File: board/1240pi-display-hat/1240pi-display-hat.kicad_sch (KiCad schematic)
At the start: 7 parts, among them J1 SFV10R-1ST, P208 Header, P415 Header, U1 74F126, U208 74F04, U415 74S74

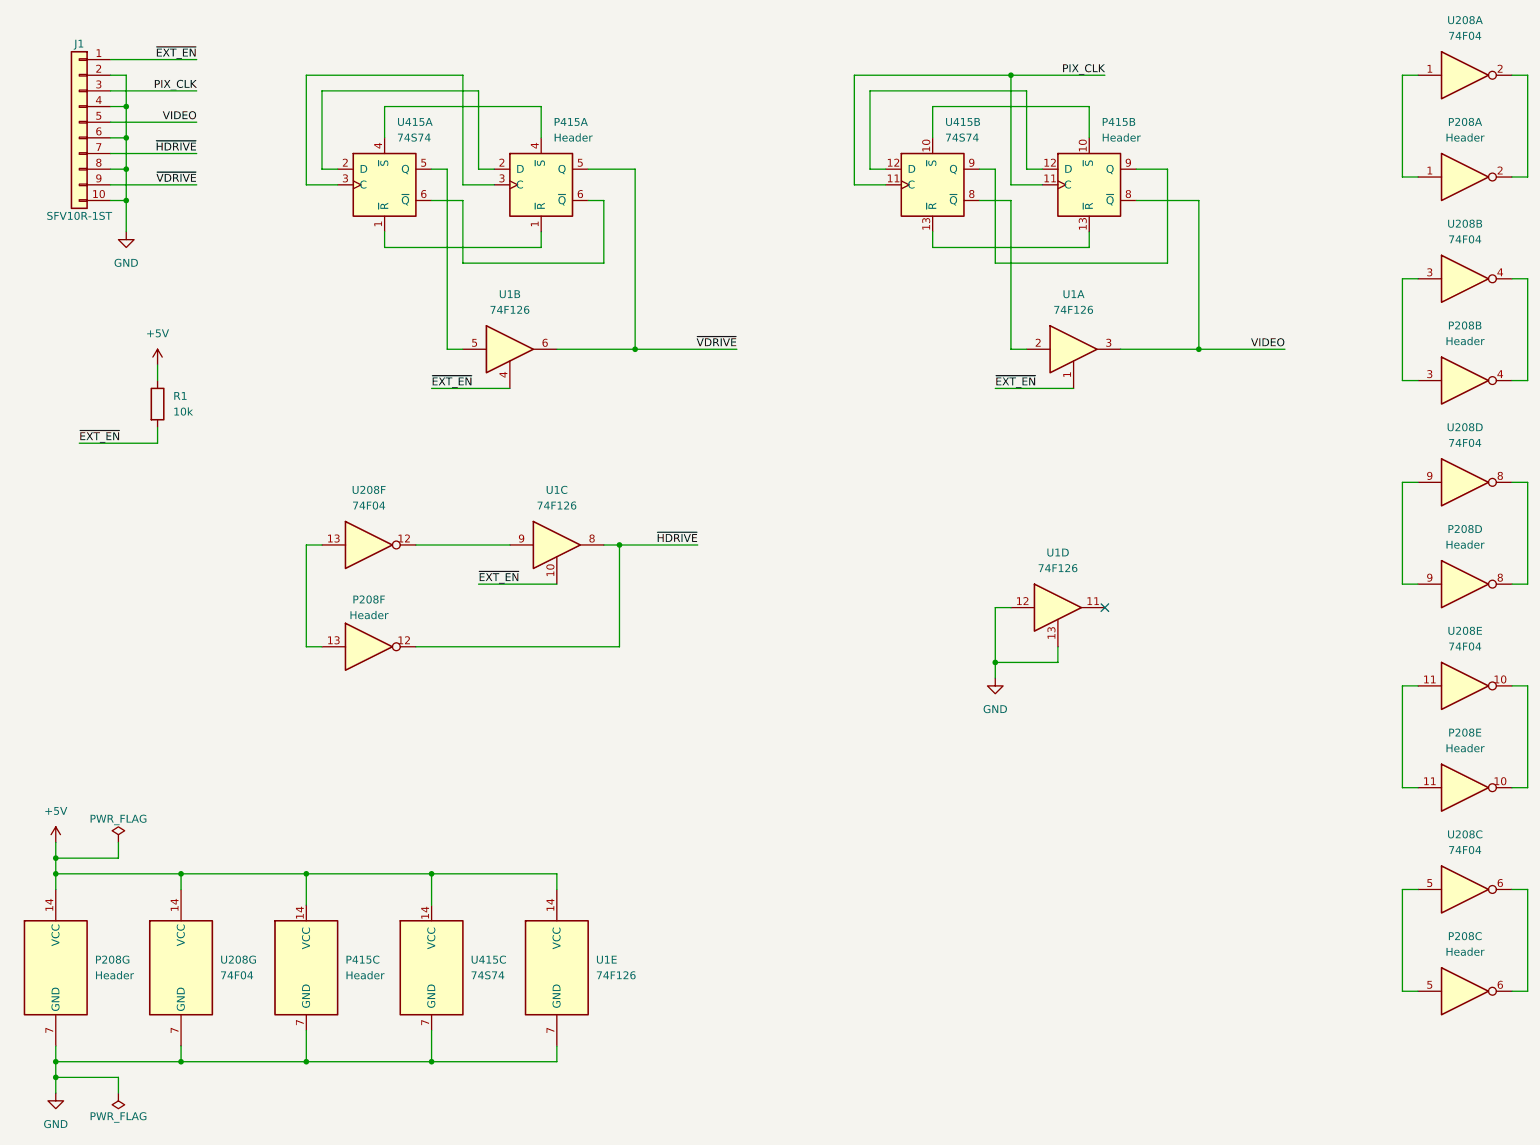
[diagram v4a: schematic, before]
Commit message: Use correct pin of U208 in display hay.
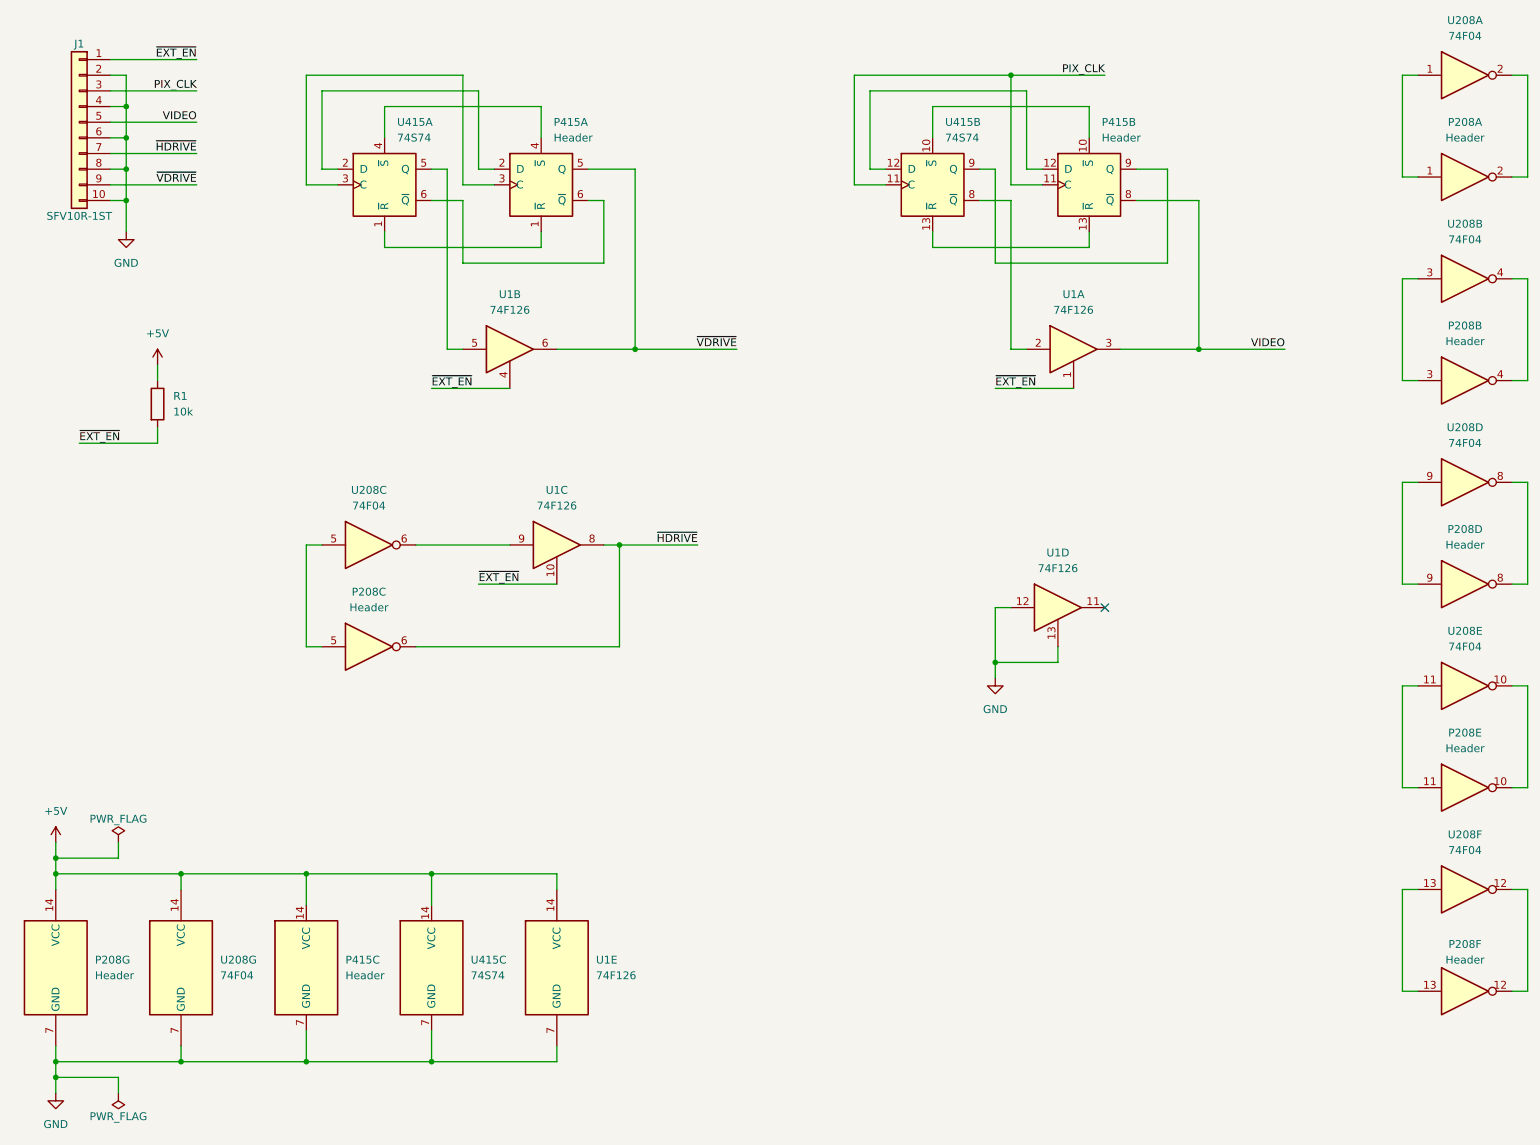
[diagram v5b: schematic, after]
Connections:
- net ~{HDRIVE}: now also P208.6; no longer P208.12
- net at U208.6: now also U1.9; no longer P208.6
- net at U208.12: now also P208.12; no longer U1.9
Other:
- moved on the sheet: P208C, P208F, U208C, U208F

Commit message: Convert display board hat to 3v3.
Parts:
- added C101, C102: 22u, Capacitor_SMD:C_0805_2012Metric, symbol Device:C_Small
- added U101: AP1117-33, Package_TO_SOT_SMD:SOT-223-3_TabPin2, symbol Regulator_Linear:AP1117-33
- U1: value 74F126 -> 74LVC126; footprint Package_DIP:DIP-14_W7.62mm -> Package_SO:SO-14_3.9x8.65mm_P1.27mm
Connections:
- net +5V: now also C101.1, U101.3 (VI); no longer U1.14 (VCC)
- net GND: now also C101.2, C102.2, U101.1 (GND); no longer U1.12
- net PIX_CLK: now also U1.12; no longer J1.3 (Pin_3)
- net PIX_CLK_O: now reaches U1.11
- net PIX_CLK_O: now also J1.3 (Pin_3)
- new net +3V3: C102.1, U1.14 (VCC), U101.2 (VO)
- no-connect marks 1 -> 0
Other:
- moved on the sheet: J1
